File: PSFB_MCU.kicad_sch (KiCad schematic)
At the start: 104 parts

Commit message: VER1.0: убрал лишнее, добавил на схему питание 5В
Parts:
- removed C10, C4: 56p, Capacitor_SMD:C_0603_1608Metric_Pad1.08x0.95mm_HandSolder, symbol Device:C_Small
- removed C18, C22: 10u, Capacitor_SMD:C_0805_2012Metric_Pad1.18x1.45mm_HandSolder, symbol Device:C_Small
- removed C19: 100u, Capacitor_Tantalum_SMD:CP_EIA-3528-21_Kemet-B_HandSolder, symbol Device:C_Polarized_Small_US
- removed C36, C46, C47, C51, C52, C53, C55, C56, C57: 100n, Capacitor_SMD:C_0603_1608Metric_Pad1.08x0.95mm_HandSolder, symbol Device:C_Small
- removed C40, C43, C44, C45: 1n, Capacitor_SMD:C_0603_1608Metric_Pad1.08x0.95mm_HandSolder, symbol Device:C_Small
- removed C58, C6: 2.2u, Capacitor_SMD:C_0603_1608Metric_Pad1.08x0.95mm_HandSolder, symbol Device:C_Small
- removed D1: ~, Package_SO:SOIC-8_3.9x4.9mm_P1.27mm, symbol CAN_My:SIT65HVD232DR
- removed D10, D3, D8, D9: ~, Package_TO_SOT_SMD:SOT-23-3, symbol Power_Protection:ESDA5V3L
- removed D2: ~, Package_TO_SOT_SMD:SOT-23, symbol Power_Protection:NUP2105L
- removed D4: ~, LED_SMD:LED_0603_1608Metric_Pad1.05x0.95mm_HandSolder, symbol Device:LED_Small
- removed D5: ~, Diode_SMD:D_SMA, symbol Device:D_Schottky_Small
- removed D6: ~, Diode_SMD:D_SOD-323_HandSoldering, symbol Device:D_Schottky_Small
- removed F2: ~, Fuse:Fuse_0805_2012Metric_Pad1.15x1.40mm_HandSolder, symbol Device:Fuse_Small
- removed FB1, FB2: ~, Inductor_SMD:L_0805_2012Metric_Pad1.05x1.20mm_HandSolder, symbol Device:FerriteBead
- removed J2: ~, TE_my:22150790, symbol 2-215079-0:2-215079-0
- removed J3, J4: ~, PLD_my:PLD16_2.0mm, symbol Connector_Generic:Conn_01x16
- removed L1: 47u, Inductor_SMD:L_1812_4532Metric_Pad1.30x3.40mm_HandSolder, symbol Device:L_Small
- removed L2: 2.2u, Inductor_SMD:L_1210_3225Metric_Pad1.42x2.65mm_HandSolder, symbol Device:L_Small
- removed R3: 120, Resistor_SMD:R_0603_1608Metric_Pad0.98x0.95mm_HandSolder, symbol Device:R_Small
- removed R37, R51, R54, R57, R60, R62, R63, R66: 3.6k, Resistor_SMD:R_0603_1608Metric_Pad0.98x0.95mm_HandSolder, symbol Device:R_Small
- removed R4: 1k, Resistor_SMD:R_0603_1608Metric_Pad0.98x0.95mm_HandSolder, symbol Device:R_Small
- removed R41, R43, R45: 8.2k, Resistor_SMD:R_0603_1608Metric_Pad0.98x0.95mm_HandSolder, symbol Device:R_Small
- removed R42, R44, R46: 36k, Resistor_SMD:R_0603_1608Metric_Pad0.98x0.95mm_HandSolder, symbol Device:R_Small
- removed R50, R52, R53, R55, R56, R58, R59, R61, R65: 1.8k, Resistor_SMD:R_0603_1608Metric_Pad0.98x0.95mm_HandSolder, symbol Device:R_Small
- removed R64: 3.3k, Resistor_SMD:R_0603_1608Metric_Pad0.98x0.95mm_HandSolder, symbol Device:R_Small
- removed U14, U15, U16: ~, Package_TO_SOT_SMD:SOT-23-5_HandSoldering, symbol Amplifier_Operational:LMV321
- removed U2: ~, Package_SO:SOIC-8_3.9x4.9mm_P1.27mm, symbol Regulator_Switching:LM2594HVM-12
- added C13, C16, C24: 10u, Capacitor_SMD:C_1206_3216Metric_Pad1.33x1.80mm_HandSolder, symbol Device:C_Small
- added C14: 0.1u, Capacitor_SMD:C_1206_3216Metric_Pad1.33x1.80mm_HandSolder, symbol Device:C_Small
- added C15: 10n, Capacitor_SMD:C_0805_2012Metric_Pad1.18x1.45mm_HandSolder, symbol Device:C_Small
- added C25: 220u, Capacitor_THT:CP_Radial_D12.5mm_P5.00mm, symbol Device:C_Polarized_Small
- added C26: 330u, Capacitor_THT:CP_Radial_D12.5mm_P5.00mm, symbol Device:C_Polarized_Small
- added C27, C28: 1n, Capacitor_THT:C_Disc_D7.5mm_W5.0mm_P10.00mm, symbol Device:C_Small
- added D3: TD301MCANFD, MORNSUN:TD5(3)01MCANFD, symbol MORNSUN:TD5(3)01MCANFD
- added D4: (no value), Package_TO_SOT_SMD:SOT-23, symbol Power_Protection:NUP2105L
- added D5: (no value), LED_SMD:LED_0805_2012Metric, symbol Device:LED_Small
- added D6: URB2405S-6WR3, MORNSUN:URB_S-6WR3, symbol MORNSUN:URB_S-6WR3
- added FL1: SRF0905-471Y, Inductor_SMD:L_CommonMode_Wuerth_WE-SL2, symbol Filter:Choke_CommonMode_PulseElectronics_PH9455x205NL
- added L1: (no value), Inductor_SMD:L_CommonModeChoke_TDK_ACM2520-2P, symbol Device:L_Coupled_Small
- added R5, R7: 59, Resistor_SMD:R_0805_2012Metric_Pad1.20x1.40mm_HandSolder, symbol Device:R_Small
- added R8: 750, Resistor_SMD:R_0805_2012Metric_Pad1.20x1.40mm_HandSolder, symbol Device:R_Small
- added U3: TLV1117LV33DCYR, Package_TO_SOT_SMD:SOT-223-3_TabPin2, symbol Regulator_Linear:LM1117MP-3.3
- C17, C23: footprint Capacitor_SMD:C_0805_2012Metric_Pad1.18x1.45mm_HandSolder -> Capacitor_SMD:C_1206_3216Metric_Pad1.33x1.80mm_HandSolder
- D1: renamed from D11; value ~ -> (none)
- D2: renamed from D7; value ~ -> (none)
- F1: value ~ -> SF-1206S100-2; footprint Fuse:Fuse_0805_2012Metric_Pad1.15x1.40mm_HandSolder -> Fuse:Fuse_1206_3216Metric; Description P/N Fuse -> (none); Product Name MF-PSMF050X-2 -> (none)
- U1, Y1: value ~ -> (none)
- U2: renamed from U10; value ~ -> (none)
- U4: renamed from U11; value ~ -> (none)
- U5: renamed from U13; value ~ -> (none)
- U6: renamed from U12; value ~ -> (none)
- renumbered C21 to C10, C33 to C11, C37 to C12, C34 to C18, C39 to C19, C35 to C20, C41 to C21, C54 to C22, C8 to C3, C9 to C4, C12 to C5, C13 to C6, C14 to C7, C15 to C8, C20 to C9, R36 to R10, R38 to R11, R39 to R12, R6 to R3, R32 to R4, R34 to R6, R35 to R9
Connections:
- net +3.3V: now also C17.2, C13.1, C14.1, D3.4 (VCC), D5.2 (A), U3.2 (VO)
- net +5V: now also C16.2, U3.3 (VI); no longer C17.1, C23.1
- net CAN1_RXD_MCU: now also D3.1 (RXD)
- net CAN1_TXD_MCU: now also D3.2 (TXD)
- net CANH: now also D4.1 (K), L1.4
- net CANL: now also D4.2 (K), L1.3
- net GND: now also C17.1, C13.2, C14.2, C16.1, D3.3 (GND), R8.2, U3.1 (GND); no longer C17.2, C23.2
- net CAN_Power: no longer names the net of F1.2
- net CAN_Power: now also C24.2, C25.1, FL1.1
- new net: C23.1, C26.2, C27.2, D6.1 (GND), FL1.3
- new net: C23.2, C26.1, C28.1, D6.2 (Vin), FL1.4
- new net: D5.1 (K), R8.1
- new net: C28.2, D6.6 (+Vo)
- new net: C27.1, D6.7 (0V)
- new net: D3.6 (CANL), L1.2, R7.1
- new net: C15.1, R5.1, R7.2
- new net: C24.1, C25.2, FL1.2
- new net: D3.7 (CANH), L1.1, R5.2
- new net GND_CAN: C15.2, D3.5 (CANG), D4.3 (A)
- no-connect marks 13 -> 11
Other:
- note removed: "+5В для внешнего CAN"
- note removed: "+5В для датчиков"
- note removed: "Вход/Выход 1"
- note removed: "Вход/Выход 2"
- note removed: "Вход/Выход 3"
- note removed: "Вход/Выход 4"
- note removed: "Датчик Холла 1"
- note removed: "Датчик Холла 2"
- note removed: "Дтчик Холла 3"
- note removed: "Измерение +5V"
- note removed: "Напряжение батареи"
- note removed: "Температура мотора"
- note removed: "Температура транзисторов"

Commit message: VER1.0: убрал лишние сигналы и доделал 5В
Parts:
- removed C11, C18, C20: 100n, Capacitor_SMD:C_0603_1608Metric_Pad1.08x0.95mm_HandSolder, symbol Device:C_Small
- removed C12, C19, C21: 1n, Capacitor_SMD:C_0603_1608Metric_Pad1.08x0.95mm_HandSolder, symbol Device:C_Small
- removed R10, R12, R6: 3.6k, Resistor_SMD:R_0603_1608Metric_Pad0.98x0.95mm_HandSolder, symbol Device:R_Small
- removed R11, R4, R9: 1.8k, Resistor_SMD:R_0603_1608Metric_Pad0.98x0.95mm_HandSolder, symbol Device:R_Small
- removed U2, U4, U5: (no value), Package_TO_SOT_SMD:SOT-23-5_HandSoldering, symbol Amplifier_Operational:LMV321
- added C29: 22u, Capacitor_THT:CP_Radial_D5.0mm_P2.00mm, symbol Device:C_Polarized_Small
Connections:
- net +5V: now also C28.2, D6.6 (+Vo), C29.1
- net GND: now also C27.1, D6.7 (0V), C29.2
- net GND1: now reaches C24.1, C25.2, FL1.2
- net +15V: now reaches F1.1
- net +5V_sense_MCU: no longer names the net of U1.8 (PC0)
- net AnalogIN1_MCU: no longer names the net of U1.20 (PA4)
- net AnalogIN2_MCU renamed PWM1_L_2
- net AnalogIN3_MCU renamed BkIN_2
- net AnalogIN4_MCU: no longer names the net of U1.23 (PA7)
- net BkIN renamed BkIN_1
- net Current_A_MCU: no longer names the net of U1.9 (PC1)
- net Current_B_MCU: no longer names the net of U1.10 (PC2)
- net Current_C_MCU: no longer names the net of U1.11 (PC3)
- net DigIN1_MCU: no longer names the net of U1.17 (PA3)
- net DigIN2_MCU renamed PWM3_L_2
- net DigIN3_MCU: no longer names the net of U1.28 (PB2)
- net DigIN4_MCU: no longer names the net of U1.29 (PB10)
- net Hall1_MCU: no longer names the net of U1.15 (PA1)
- net Hall2_MCU: no longer names the net of U1.16 (PA2)
- net Hall3_MCU: no longer names the net of U1.14 (PA0)
- net PWM1_H renamed PWM1_H_1
- net PWM1_L renamed PWM1_L_1
- net PWM2_H renamed PWM2_H_1
- net PWM2_L renamed PWM2_L_1
- net PWM3_H renamed PWM3_H_1
- net PWM3_L renamed PWM3_L_1
- net Temp_mosfet_sense_MCU renamed PWM2_L_2
- net Temp_motor_sense_MCU: no longer names the net of U1.25 (PC5)
- net VBAT_sense_MCU: no longer names the net of U1.24 (PC4)
- net f1H: no longer names the net of U1.44 (PA11)
- net f1L: no longer names the net of U1.45 (PA12)
- net f2H renamed PWM3_H_2
- net f2L: no longer names the net of U1.40 (PC9)
- net f3H renamed PWM2_H_2
- net f3L renamed PWM1_H_2
- net uC_drv_en: no longer names the net of U1.58 (PB6)
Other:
- note added: "Питание 5В"
- note removed: "Измерение тока фазы B"
- note removed: "Измерение тока фазы C"
- note removed: "Измерение тока фазы А"
- moved on the sheet: C13, C14, C15, C16, C17, C22, C23, C24, C25, C26, C27, C28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

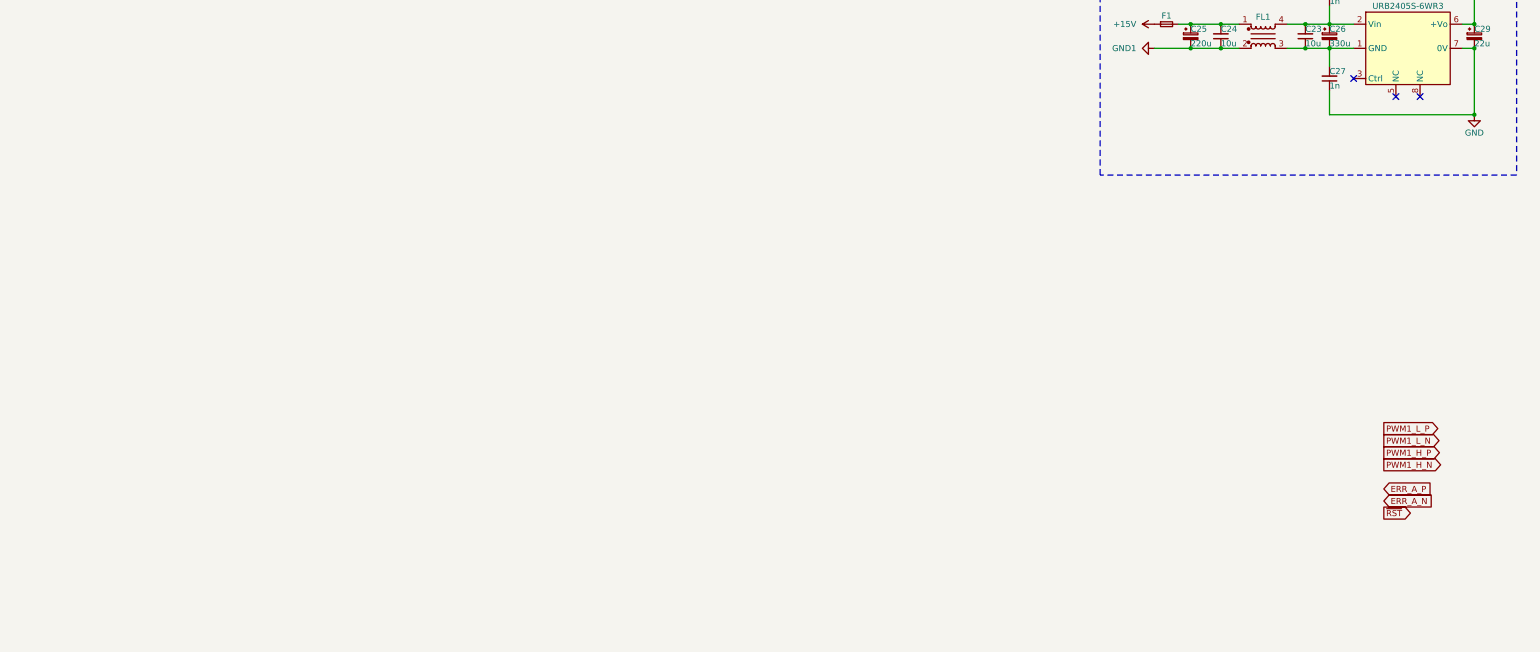
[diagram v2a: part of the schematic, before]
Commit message: VER1.0: надо разобраться с питанием 9-60В
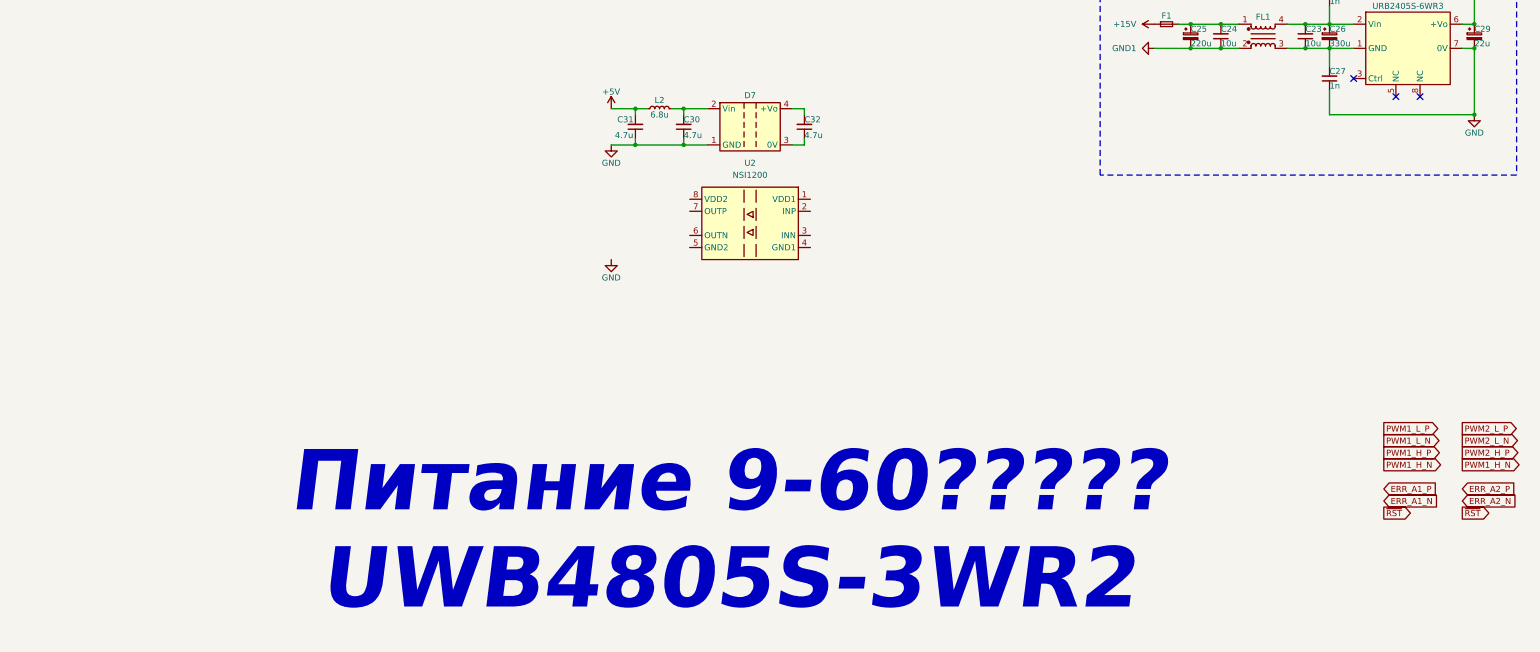
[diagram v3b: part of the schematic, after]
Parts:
- added C30, C31, C32: 4.7u, Capacitor_SMD:C_1206_3216Metric_Pad1.33x1.80mm_HandSolder, symbol Device:C_Small
- added D7: B1505S-1WR3, MORNSUN:B_S-1WR3, symbol MORNSUN:B_S-1WR3
- added L2: 6.8u, symbol Device:L_Small
- added U2: NSI1200, Package_SO:SOIC-8_3.9x4.9mm_P1.27mm, symbol Isolator:ADuM1200AR
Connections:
- net +5V: now also C31.2, L2.1
- net GND: now also C30.1, C31.1, D7.1 (GND)
- new net: C30.2, D7.2 (Vin), L2.2
- new net: C32.1, D7.3 (0V)
- new net: C32.2, D7.4 (+Vo)
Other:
- note added: "Питание 9-60????? UWB4805S-3WR2"

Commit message: VER1.0: собрал всю цепь питания на схеме
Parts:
- removed C24: 10u, Capacitor_SMD:C_1206_3216Metric_Pad1.33x1.80mm_HandSolder, symbol Device:C_Small
- removed C25: 220u, Capacitor_THT:CP_Radial_D12.5mm_P5.00mm, symbol Device:C_Polarized_Small
- removed C26: 330u, Capacitor_THT:CP_Radial_D12.5mm_P5.00mm, symbol Device:C_Polarized_Small
- removed C27, C28: 1n, Capacitor_THT:C_Disc_D7.5mm_W5.0mm_P10.00mm, symbol Device:C_Small
- removed C29: 22u, Capacitor_THT:CP_Radial_D5.0mm_P2.00mm, symbol Device:C_Polarized_Small
- removed C30, C31, C32: 4.7u, Capacitor_SMD:C_1206_3216Metric_Pad1.33x1.80mm_HandSolder, symbol Device:C_Small
- removed D6: URB2405S-6WR3, MORNSUN:URB_S-6WR3, symbol MORNSUN:URB_S-6WR3
- removed D7: B1505S-1WR3, MORNSUN:B_S-1WR3, symbol MORNSUN:B_S-1WR3
- removed F1: SF-1206S100-2, Fuse:Fuse_1206_3216Metric, symbol Device:Fuse_Small
- removed FL1: SRF0905-471Y, Inductor_SMD:L_CommonMode_Wuerth_WE-SL2, symbol Filter:Choke_CommonMode_PulseElectronics_PH9455x205NL
- removed L2: 6.8u, symbol Device:L_Small
- removed U2: NSI1200, Package_SO:SOIC-8_3.9x4.9mm_P1.27mm, symbol Isolator:ADuM1200AR
- added C11: 1u, Capacitor_SMD:C_0805_2012Metric_Pad1.18x1.45mm_HandSolder, symbol Device:C_Small
- added C12: 220p, Capacitor_SMD:C_0805_2012Metric_Pad1.18x1.45mm_HandSolder, symbol Device:C_Small
- added C18, C35, C36, C37, C39: 100n, Capacitor_SMD:C_0805_2012Metric_Pad1.18x1.45mm_HandSolder, symbol Device:C_Small
- added C19: 47p, Capacitor_SMD:C_0805_2012Metric_Pad1.18x1.45mm_HandSolder, symbol Device:C_Small
- added C20: 1n, Capacitor_SMD:C_0805_2012Metric_Pad1.18x1.45mm_HandSolder, symbol Device:C_Small
- added C21: 33n, Capacitor_SMD:C_0805_2012Metric_Pad1.18x1.45mm_HandSolder, symbol Device:C_Small
- added C33: 560p, Capacitor_SMD:C_0805_2012Metric_Pad1.18x1.45mm_HandSolder, symbol Device:C_Small
- added C34: 100u, Capacitor_THT:CP_Radial_D10.0mm_P5.00mm, symbol Device:C_Polarized_Small
- added C38: 220u, Capacitor_THT:CP_Radial_D8.0mm_P3.50mm, symbol Device:C_Polarized_Small
- added C40: 4.7u, Capacitor_SMD:C_1210_3225Metric_Pad1.33x2.70mm_HandSolder, symbol Device:C_Small
- added C45, C46, C47, C48, C49: 10u, Capacitor_SMD:C_1210_3225Metric_Pad1.33x2.70mm_HandSolder, symbol Device:C_Small
- added D10, D11, D12: D_Schottky_Small, Diode_SMD:D_SMA_Handsoldering, symbol Device:D_Schottky_Small
- added D6: K7809T, MORNSUN:K78xxT-1000R3, symbol MORNSUN:K78xxT-500R3 _1000R3
- added D7, D9: (no value), LED_SMD:LED_0805_2012Metric, symbol Device:LED_Small
- added D8: URB2415LD-20WR3, MORNSUN:URB_LD-20WR3, symbol MORNSUN:URB_LD-20WR3
- added L3: 10u, Inductor_SMD:L_Panasonic_PCC-M1040ML, symbol Device:L
- added Q1, Q2, Q3, Q4: WMM043N10HGD, Package_TO_SOT_SMD:TO-263-2, symbol Transistor_FET:IRFS4115
- added R10: 10m, Resistor_SMD:R_2512_6332Metric_Pad1.40x3.35mm_HandSolder, symbol Device:R_Small
- added R11: 143k, Resistor_SMD:R_0805_2012Metric_Pad1.20x1.40mm_HandSolder, symbol Device:R_Small
- added R12, R17, R21: 10k, Resistor_SMD:R_0805_2012Metric_Pad1.20x1.40mm_HandSolder, symbol Device:R_Small
- added R13: 59k, Resistor_SMD:R_0805_2012Metric_Pad1.20x1.40mm_HandSolder, symbol Device:R_Small
- added R14: 249k, Resistor_SMD:R_0805_2012Metric_Pad1.20x1.40mm_HandSolder, symbol Device:R_Small
- added R15: 10, Resistor_SMD:R_0805_2012Metric_Pad1.20x1.40mm_HandSolder, symbol Device:R_Small
- added R16: 2k, Resistor_SMD:R_0805_2012Metric_Pad1.20x1.40mm_HandSolder, symbol Device:R_Small
- added R18, R24: 0, Resistor_SMD:R_0805_2012Metric_Pad1.20x1.40mm_HandSolder, symbol Device:R_Small
- added R19: 1k, Resistor_SMD:R_0805_2012Metric_Pad1.20x1.40mm_HandSolder, symbol Device:R_Small
- added R20: 3k, Resistor_SMD:R_0805_2012Metric_Pad1.20x1.40mm_HandSolder, symbol Device:R_Small
- added R22: 240k, Resistor_SMD:R_0805_2012Metric_Pad1.20x1.40mm_HandSolder, symbol Device:R_Small
- added R23: 51k, Resistor_SMD:R_0805_2012Metric_Pad1.20x1.40mm_HandSolder, symbol Device:R_Small
- added R4: 93.1k, Resistor_SMD:R_0805_2012Metric_Pad1.20x1.40mm_HandSolder, symbol Device:R_Small
- added R6, R9: 100, Resistor_SMD:R_0805_2012Metric_Pad1.20x1.40mm_HandSolder, symbol Device:R_Small
- added U4: LM5176PWP, Package_SO:HTSSOP-28-1EP_4.4x9.7mm_P0.65mm_EP3.4x9.5mm_ThermalVias, symbol Regulator_Switching:LM5176PWP
- added U5: AMS1117-5.0, Package_TO_SOT_SMD:SOT-223-3_TabPin2, symbol Regulator_Linear:LM1117MP-3.3
- R8: value 750 -> 1k
- U3: value TLV1117LV33DCYR -> AMS1117-3.3
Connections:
- net +15V: now also C49.2, D6.1 (+Vin), D6.2 (+Vin), D8.4 (+Vo), D9.2 (A)
- net +5V: now also C23.2, D7.2 (A), U5.2 (VO)
- net CANH: now also L1.2; no longer L1.4
- net CANL: now also L1.4; no longer L1.3
- net GND: now also C23.1, C48.1, C49.1, D6.3 (GND), D6.7 (GND), R19.2, R20.2, U5.1 (GND)
- net GND1: now also D8.6 (0V), R24.2
- net at D3.6 (CANL), R7.1: now also L1.3; no longer L1.2
- new net: D9.1 (K), R20.1
- new net: R18.1, U4.13 (ISNS(-)), U4.14 (ISNS(+))
- new net: D7.1 (K), R19.1
- new net: R21.1, R23.1, U4.11 (FB)
- new net: R22.1, R23.2
- new net: C18.1, U4.8 (SS)
- new net: C36.2, D10.1 (K), U4.26 (BOOT1)
- new net: C35.1, R15.1, U4.2 (VIN)
- new net: C20.1, R11.2, U4.6 (RT/SYNC)
- new net: Q2.3 (S), Q4.3 (S), R10.2, R6.1
- new net: D12.1 (K), R15.2
- new net: R4.2, U4.4 (MODE)
- new net: C19.1, R9.2, U4.15 (CSG)
- new net: C19.2, R6.2, U4.16 (CS)
- new net: R17.1, U4.17 (PGOOD)
- new net: R13.1, R14.1, U4.1 (EN/UVLO)
- new net: D8.5 (Trim), R24.1
- new net: C21.1, C33.1, U4.9 (COMP)
- new net: C21.2, R12.2
- new net: R16.2, U4.3 (VISNS)
- new net: C37.2, D11.1 (K), U4.20 (BOOT2)
- new net: C12.1, U4.7 (SLOPE)
- new net +24V: C38.1, C39.1, C45.2, C46.2, C47.2, D8.3 (Vin), Q3.2 (D), R22.2, U4.12 (VOSNS), U4.24 (BIAS)
- new net +9V: C48.2, D6.4 (+Vout), D6.5 (+Vout), U5.3 (VI)
- new net GND_IN: C11.2, C12.2, C18.2, C33.2, C34.2, C35.2, C38.2, C39.2, C40.1, C45.1, C46.1, C47.1, D8.2 (GND), R10.1, R11.1, R12.1, R13.2, R21.2, R4.1, R9.1, U4.10 (AGND), U4.22 (PGND), U4.29 (PowerPAD), U4.5 (DITH)
- new net HDRV1: Q1.1 (G), U4.27 (HDRV1)
- new net HDRV2: Q3.1 (G), U4.19 (HDRV2)
- new net LDRV1: Q2.1 (G), U4.25 (LDRV1)
- new net LDRV2: Q4.1 (G), U4.21 (LDRV2)
- new net SW1: C36.1, L3.1, Q1.3 (S), Q2.2 (D), U4.28 (SW1)
- new net SW2: C37.1, L3.2, Q3.3 (S), Q4.2 (D), U4.18 (SW2)
- new net VCC: C11.1, D10.2 (A), D11.2 (A), R17.2, U4.23 (VCC)
- new net VIN: C34.1, C40.2, D12.2 (A), Q1.2 (D), R14.2, R16.1, R18.2
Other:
- note added: "Питание 15В"
- note added: "Питание 24В"
- note removed: "Питание 9-60????? UWB4805S-3WR2"
- moved on the sheet: C16, C17, D5, R8, U3
